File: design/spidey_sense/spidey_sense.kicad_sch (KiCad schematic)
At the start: 13 parts, among them J1 Input_Screw_Terminal, J2 Output_Screw_Terminal, J3 Thermocouple_Terminal, J4 Thermocouple_Terminal, J5 Thermocouple_Terminal, J6 Thermocouple_Terminal, U1 LT1025, U2 LTC1983-5

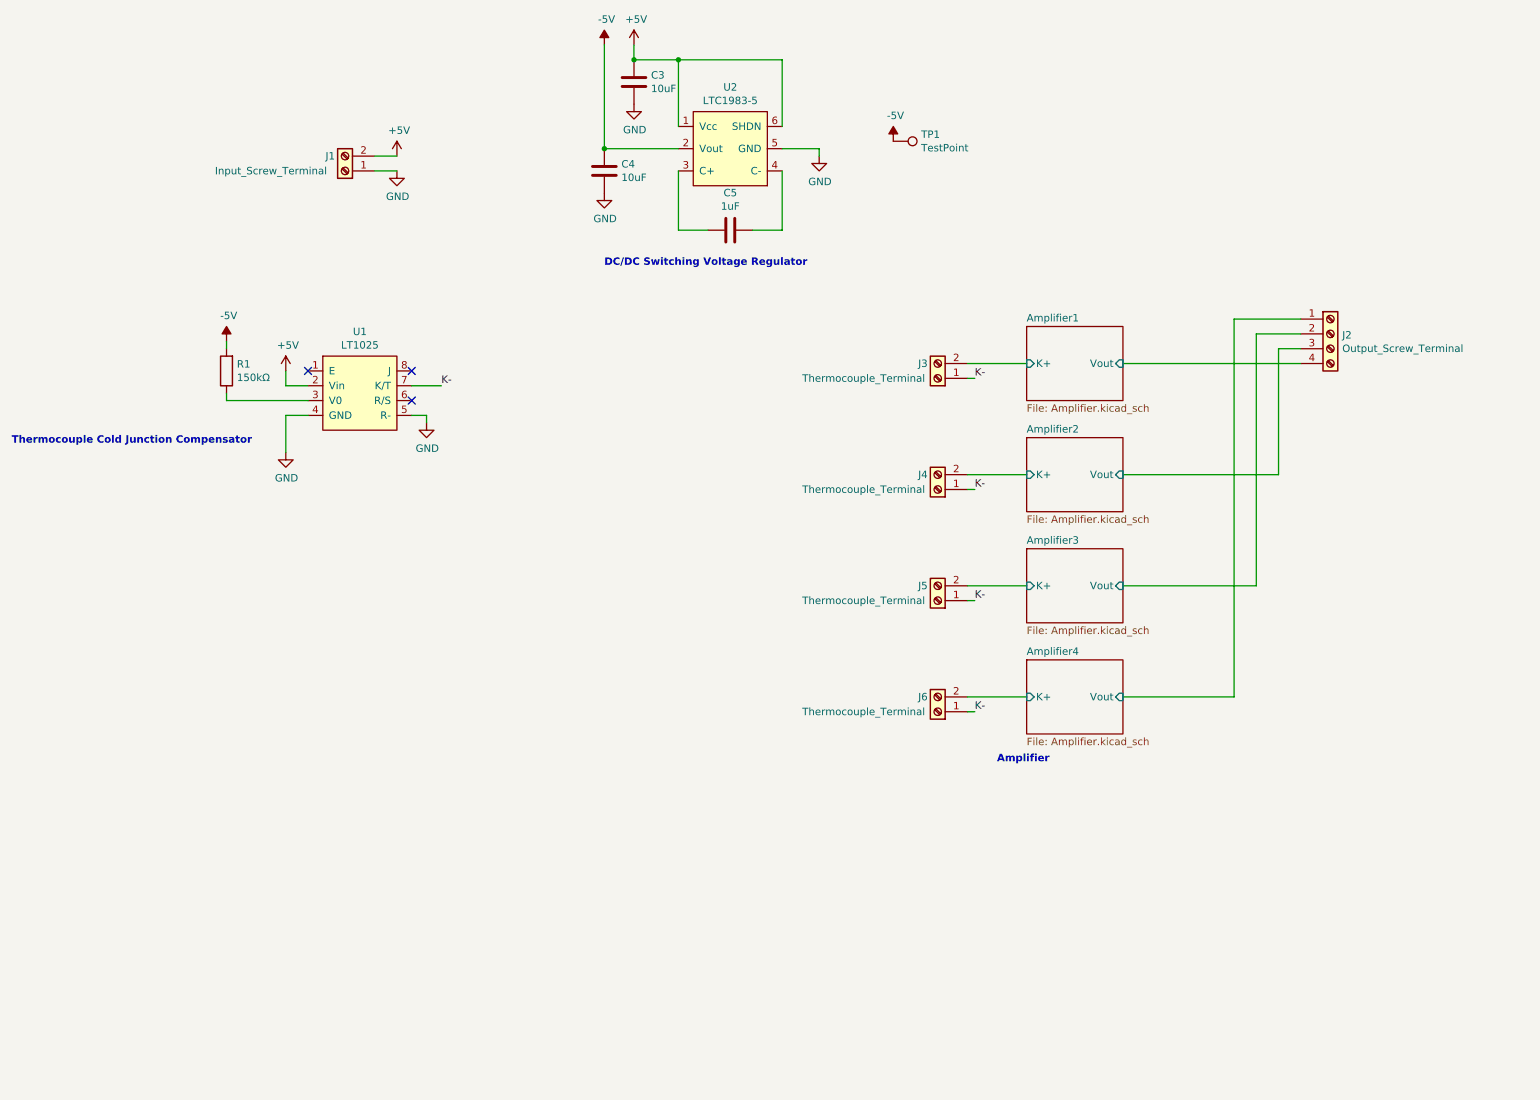
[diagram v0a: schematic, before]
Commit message: Added vias to avoid GND loops
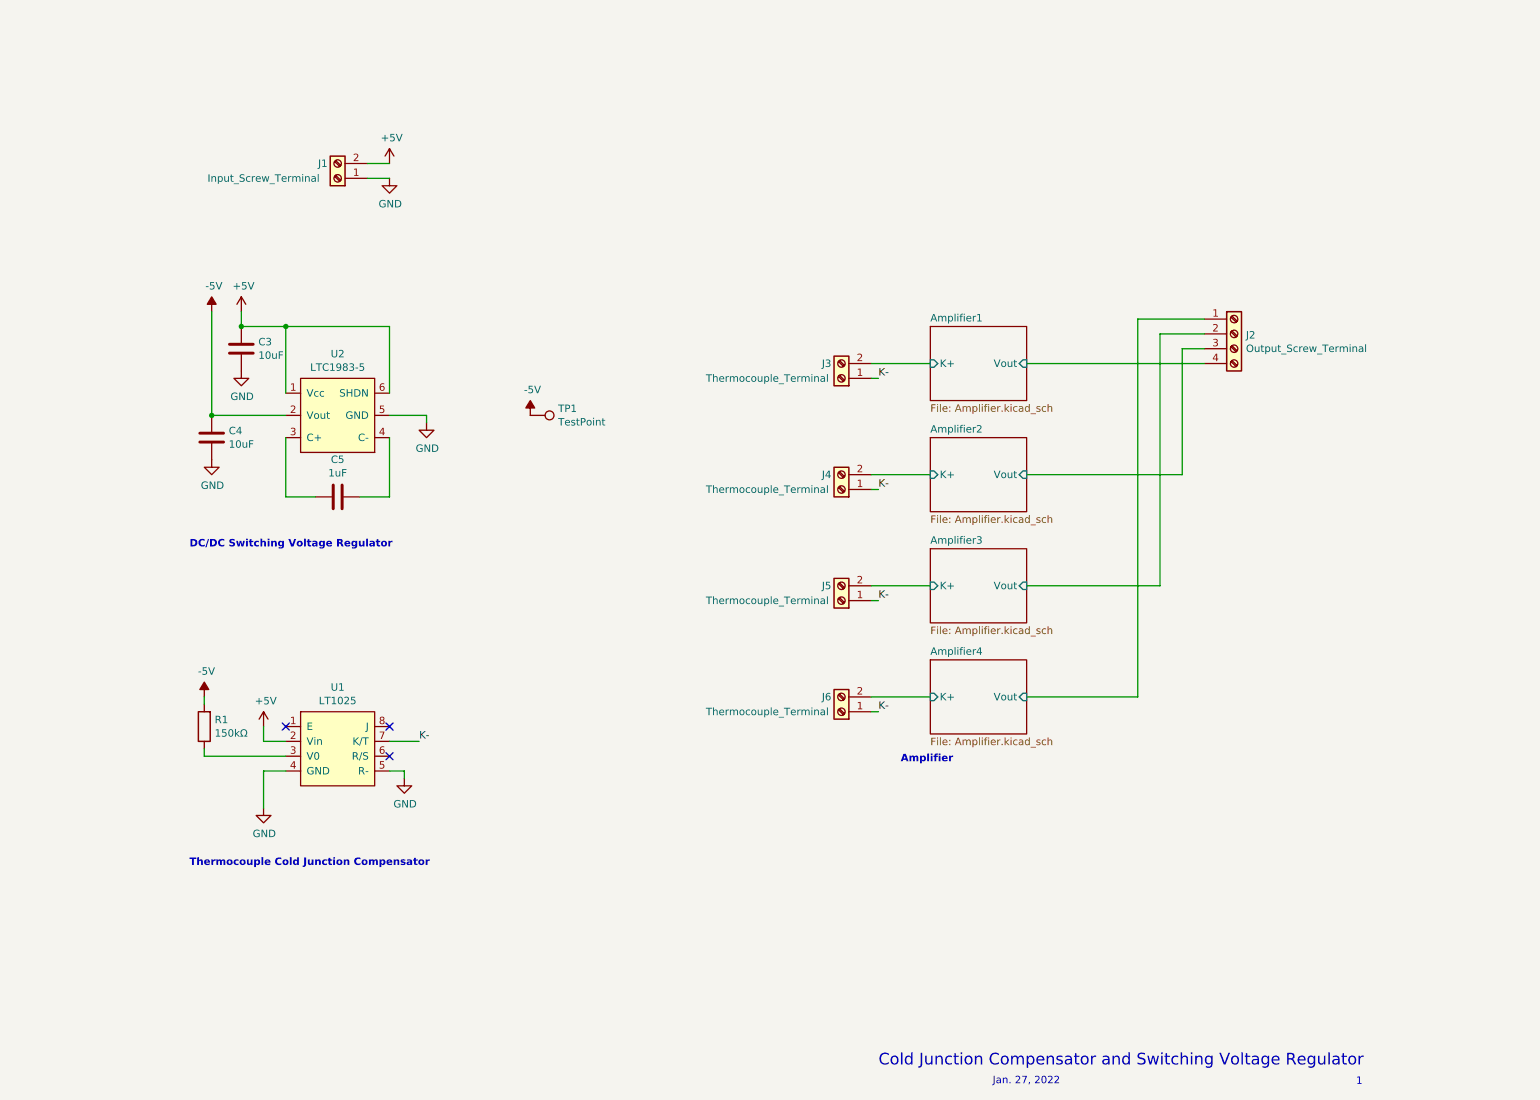
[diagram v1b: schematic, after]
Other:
- note added: "1"
- note added: "Cold Junction Compensator and Switching Voltage Regulator"
- note added: "Jan. 27, 2022"
- moved on the sheet: C3, C4, C5, J1, J2, J3, J4, J5, J6, R1, TP1, U1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

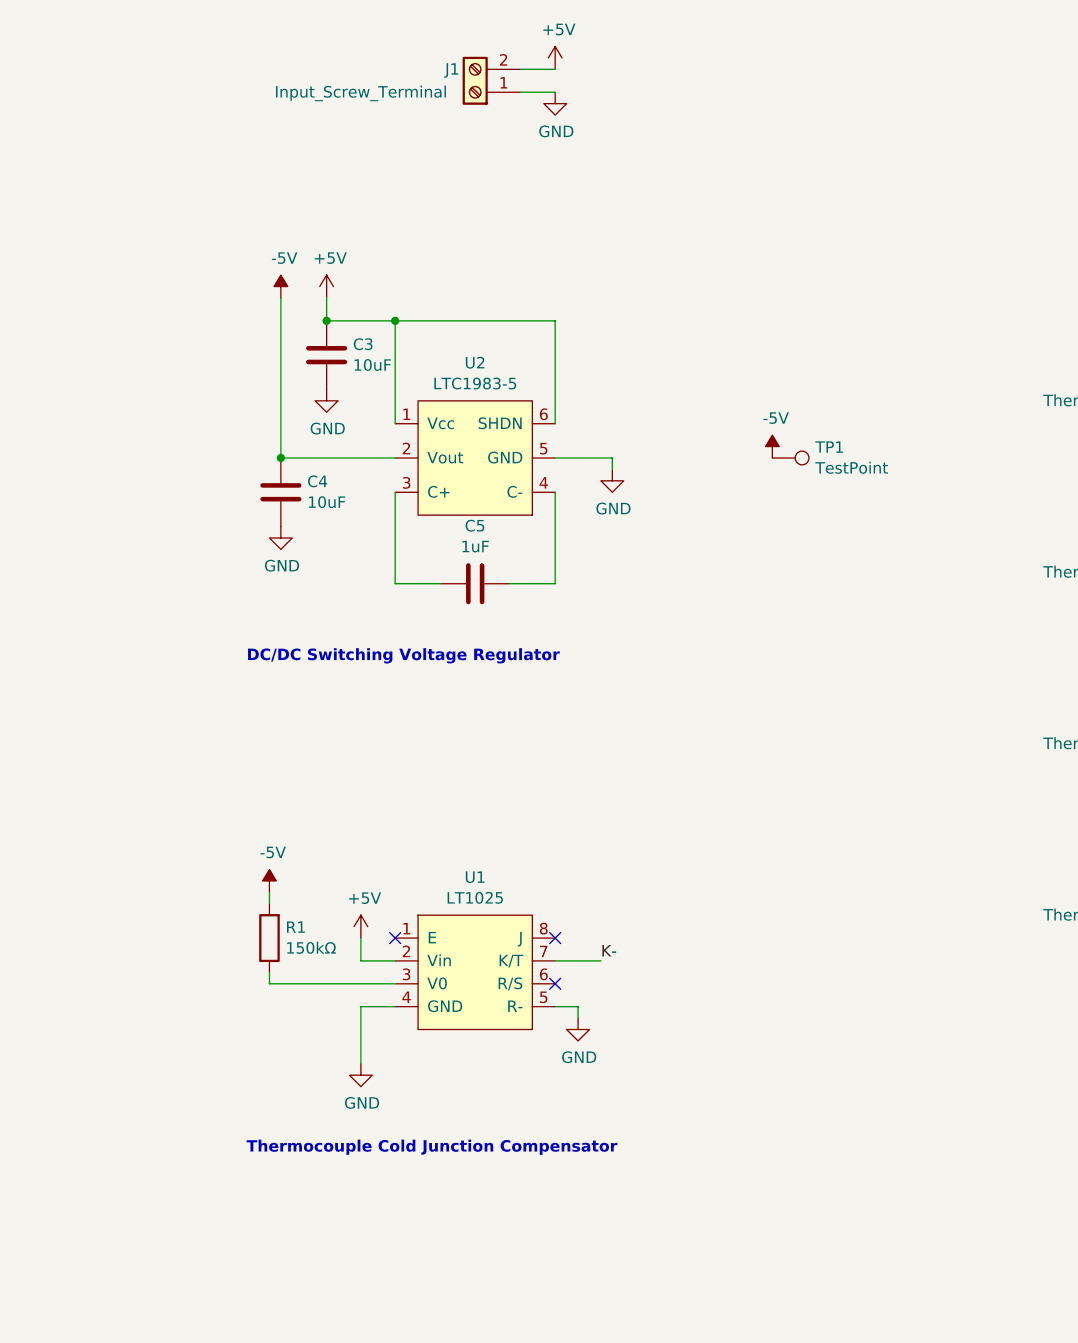
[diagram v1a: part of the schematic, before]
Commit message: Changed C5 value
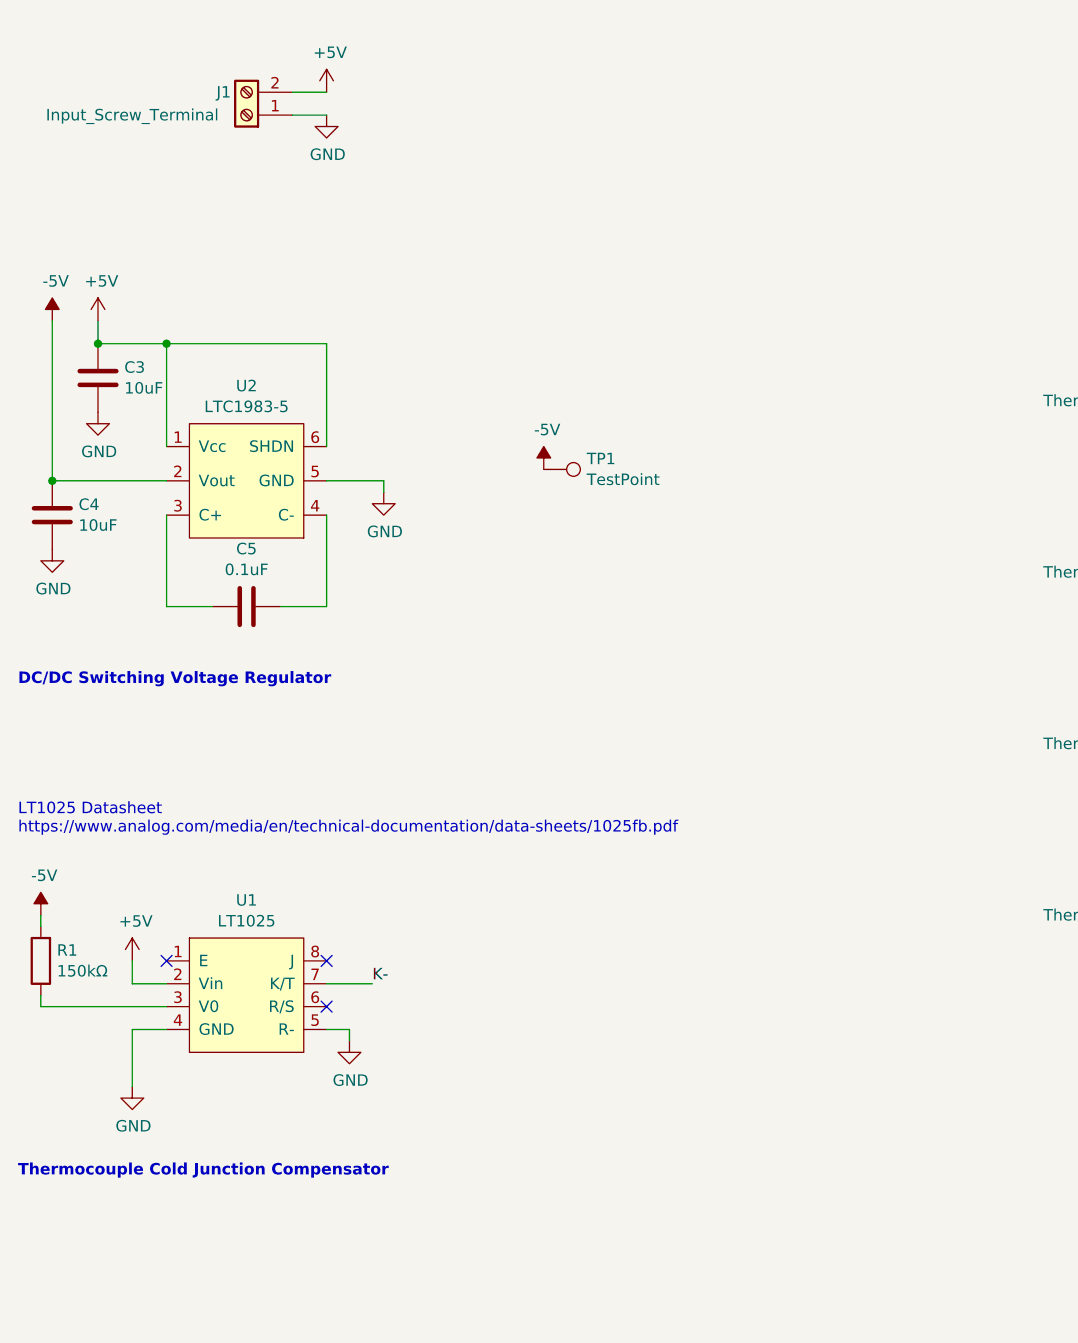
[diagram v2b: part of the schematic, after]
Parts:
- C5: value 1uF -> 0.1uF
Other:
- note added: "LT1025 Datasheet https://www.analog.com/media/en/technical-documentation/data-sheets/1025fb.pdf"
- moved on the sheet: C3, C4, C5, J1, R1, TP1, U1, U2

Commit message: Initial schematic design
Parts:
- removed C3, C4: 10uF, Capacitor_SMD:C_0805_2012Metric_Pad1.18x1.45mm_HandSolder, symbol Device:C
- removed C5: 0.1uF, Capacitor_SMD:C_0805_2012Metric_Pad1.18x1.45mm_HandSolder, symbol Device:C
- removed R1: 150kΩ, Resistor_SMD:R_0805_2012Metric_Pad1.20x1.40mm_HandSolder, symbol Device:R
- removed TP1: TestPoint, TestPoint:TestPoint_Pad_1.5x1.5mm, symbol Connector:TestPoint
- removed U1: LT1025, Package_SO:SOP-8_3.9x4.9mm_P1.27mm, symbol Thermocouple:LT1025
- removed U2: LTC1983-5, Package_SO:TSOP-6_1.65x3.05mm_P0.95mm, symbol Thermocouple:LTC1983-5
- added J6, J7, J8, J9: Conn_01x06_Female, Connector_PinSocket_2.54mm:PinSocket_1x06_P2.54mm_Vertical, symbol Connector:Conn_01x06_Female
- renumbered J2 to J10, J3 to J2, J4 to J3, J5 to J4, J6 to J5
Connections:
- net GND: now also J6.2 (Pin_2), J6.6 (Pin_6), J7.2 (Pin_2), J7.6 (Pin_6), J8.2 (Pin_2), J8.6 (Pin_6), J9.2 (Pin_2), J9.6 (Pin_6)
- net +5V renamed +24V
- net +24V: now also J6.1 (Pin_1), J7.1 (Pin_1), J8.1 (Pin_1), J9.1 (Pin_1)
- net Amplifier1/K+: no longer names the net of J2.2 (Pin_2)
- net Amplifier1/K+: now also J9.3 (Pin_3)
- net Amplifier1/Vout: no longer names the net of J10.4 (Pin_4)
- net Amplifier1/Vout: now also J9.5 (Pin_5)
- net Amplifier2/K+: no longer names the net of J3.2 (Pin_2)
- net Amplifier2/K+: now also J6.3 (Pin_3)
- net Amplifier2/Vout: no longer names the net of J10.3 (Pin_3)
- net Amplifier2/Vout: now also J6.5 (Pin_5)
- net Amplifier3/K+: no longer names the net of J4.2 (Pin_2)
- net Amplifier3/K+: now also J7.3 (Pin_3)
- net Amplifier3/Vout: no longer names the net of J10.2 (Pin_2)
- net Amplifier3/Vout: now also J7.5 (Pin_5)
- net Amplifier4/K+: no longer names the net of J5.2 (Pin_2)
- net Amplifier4/K+: now also J8.3 (Pin_3)
- net Amplifier4/Vout: no longer names the net of J10.1 (Pin_1)
- net Amplifier4/Vout: now also J8.5 (Pin_5)
- removed net K-: J2.1 (Pin_1), J3.1 (Pin_1), J4.1 (Pin_1), J5.1 (Pin_1)
- new net: J2.1 (Pin_1), J9.4 (Pin_4)
- new net: J3.1 (Pin_1), J6.4 (Pin_4)
- new net: J4.1 (Pin_1), J7.4 (Pin_4)
- new net: J5.1 (Pin_1), J8.4 (Pin_4)
- no-connect marks 3 -> 0
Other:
- removed sheet Amplifier1
- removed sheet Amplifier2
- removed sheet Amplifier3
- removed sheet Amplifier4
- note added: "4"
- note added: "Oct 11, 2022"
- note added: "Thermocouple Signal Conditioner Mounting Board"
- note removed: "1"
- note removed: "Amplifier"
- note removed: "Cold Junction Compensator and Switching Voltage Regulator"
- note removed: "DC/DC Switching Voltage Regulator"
- note removed: "Jan. 27, 2022"
- note removed: "LT1025 Datasheet https://www.analog.com/media/en/technical-documentation/data-sheets/1025fb.pdf"
- note removed: "Thermocouple Cold Junction Compensator"
- moved on the sheet: J1, J2, J3, J4, J5
